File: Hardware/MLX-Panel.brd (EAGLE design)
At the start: 62 x 62 mm, 135 parts, among them U1 MLX90393_MAGNETOMETER, U2 MLX90393_MAGNETOMETER, U3 MLX90393_MAGNETOMETER, U4 MLX90393_MAGNETOMETER, U5 MLX90393_MAGNETOMETER, U6 MLX90393_MAGNETOMETER, U7 MLX90393_MAGNETOMETER, U8 MLX90393_MAGNETOMETER, U9 MLX90393_MAGNETOMETER

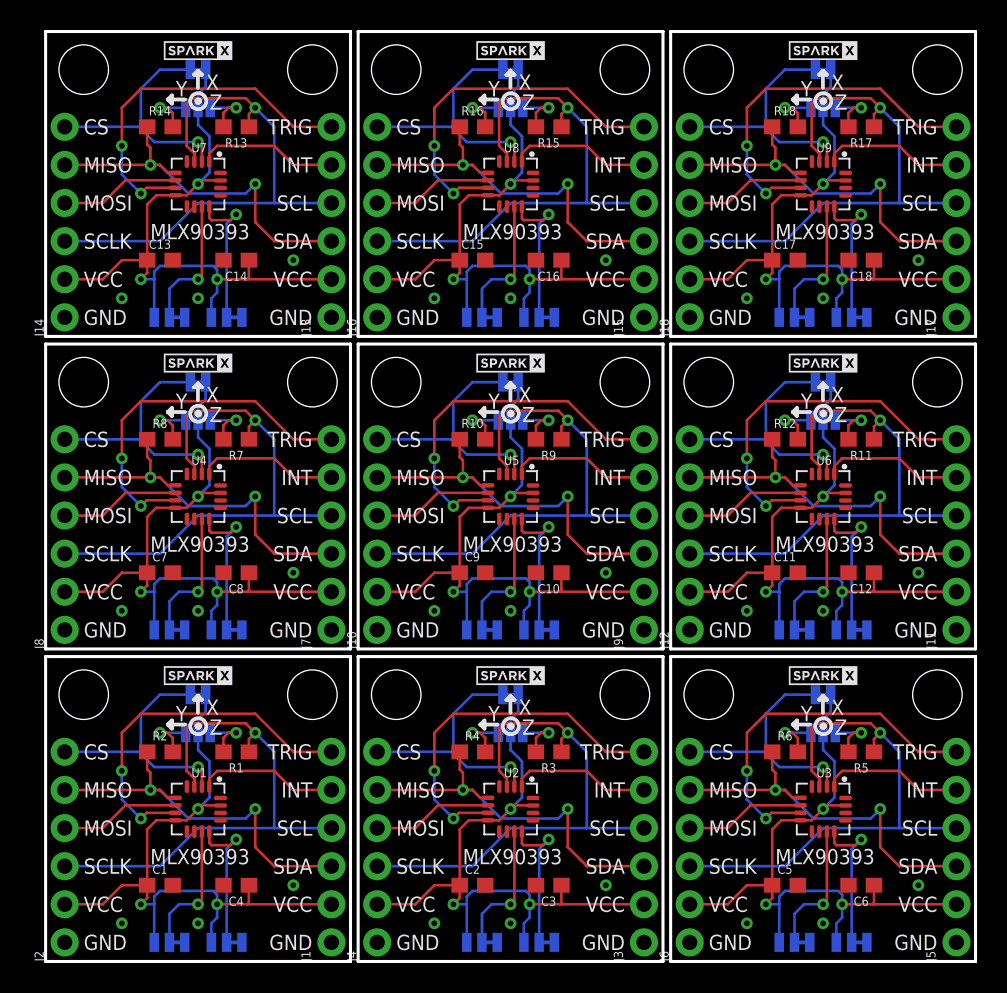
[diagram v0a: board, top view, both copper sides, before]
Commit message: Adding bottom silk
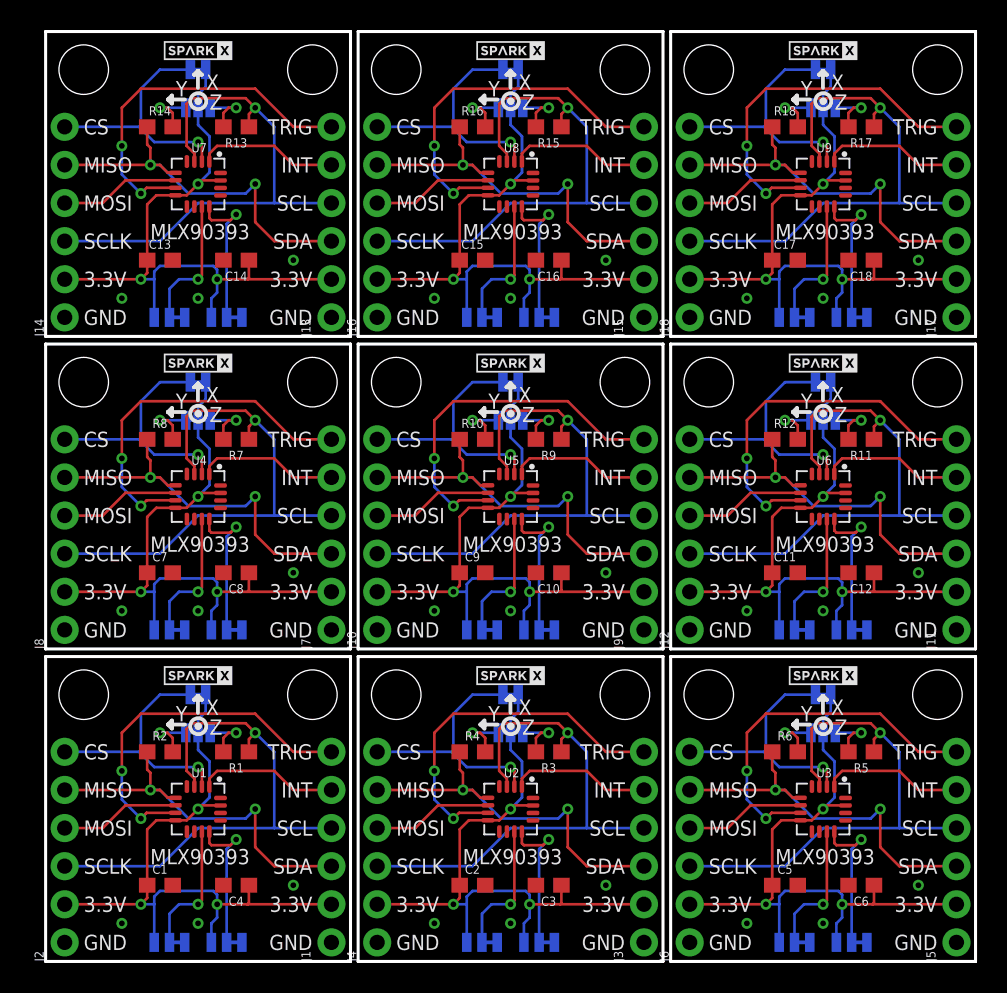
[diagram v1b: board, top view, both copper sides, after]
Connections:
- net GND renamed GND9
- net GND1 renamed GND10
- net GND2 renamed GND11
- net GND3 renamed GND12
- net GND4 renamed GND13
- net GND5 renamed GND14
- net GND6 renamed GND15
- net GND7 renamed GND16
- net GND8 renamed GND17
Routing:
- net 3.3V5: track 45.9 -> 44.9 mm
- net 3.3V4: track 45.9 -> 44.9 mm
- net 3.3V8: track 45.9 -> 44.9 mm
- net 3.3V7: track 45.9 -> 44.9 mm
- net 3.3V2: track 45.9 -> 44.9 mm
- net 3.3V6: track 45.9 -> 44.9 mm
- net 3.3V1: track 45.9 -> 44.9 mm
- net 3.3V: track 45.9 -> 44.9 mm
- net 3.3V3: track 45.9 -> 44.9 mm
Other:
- board text added: "3.3V"
- board text removed: "VCC"
